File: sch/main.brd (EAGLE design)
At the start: 99.1 x 50.8 mm, 22 parts, among them IC2 PIC16F628P, K1 TF2--5V, K2 TF2--5V, T1 BC547, T2 BC547

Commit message: Better routing
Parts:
- moved R2 26.2 mm to (77.5, 19.1), turned to 0 degrees
- moved R3 9.16 mm to (59.7, 26.7), turned to 0 degrees
- moved C3 1.80 mm to (33.0, 31.8), turned to 90 degrees
- moved T1 1.27 mm to (82.5, 22.9)
- moved T2 1.27 mm to (64.8, 22.9)
- turned C1 to 90 degrees
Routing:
- net N$9: track 99.2 -> 3.81 mm
- net SW1: track 117.0 -> 26.8 mm, vias 2 -> 0
- net GND: track 342.9 -> 263.0 mm, vias 2 -> 0
- net N$8: track 75.8 -> 3.81 mm
- net DB0: track 77.3 -> 23.7 mm
- net DB1: track 67.2 -> 16.5 mm, vias 2 -> 0
- net +5V: track 167.8 -> 129.3 mm
- net +12V: track 113.7 -> 77.4 mm, vias 4 -> 1
- net N$2: track 49.7 -> 32.2 mm, vias 2 -> 0
- net N$6: track 3.81 -> 19.4 mm
- net SW3: track 61.3 -> 48.2 mm
- net N$1: track 32.1 -> 20.6 mm
- net RS: track 44.8 -> 38.1 mm, vias 2 -> 0
- net SW2: track 38.2 -> 34.3 mm, vias 2 -> 0
- net N$7: track 3.81 -> 6.33 mm
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
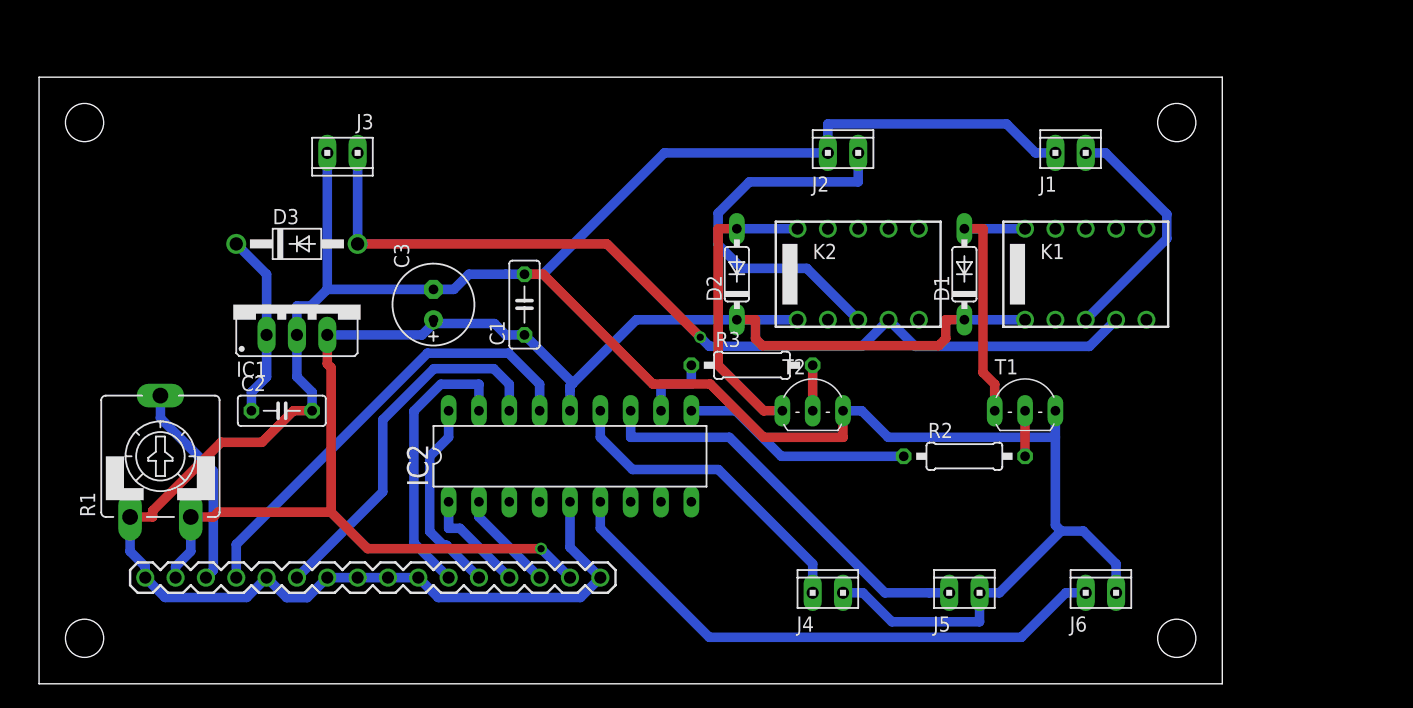
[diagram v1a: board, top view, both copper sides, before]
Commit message: Replaced relays with transistors
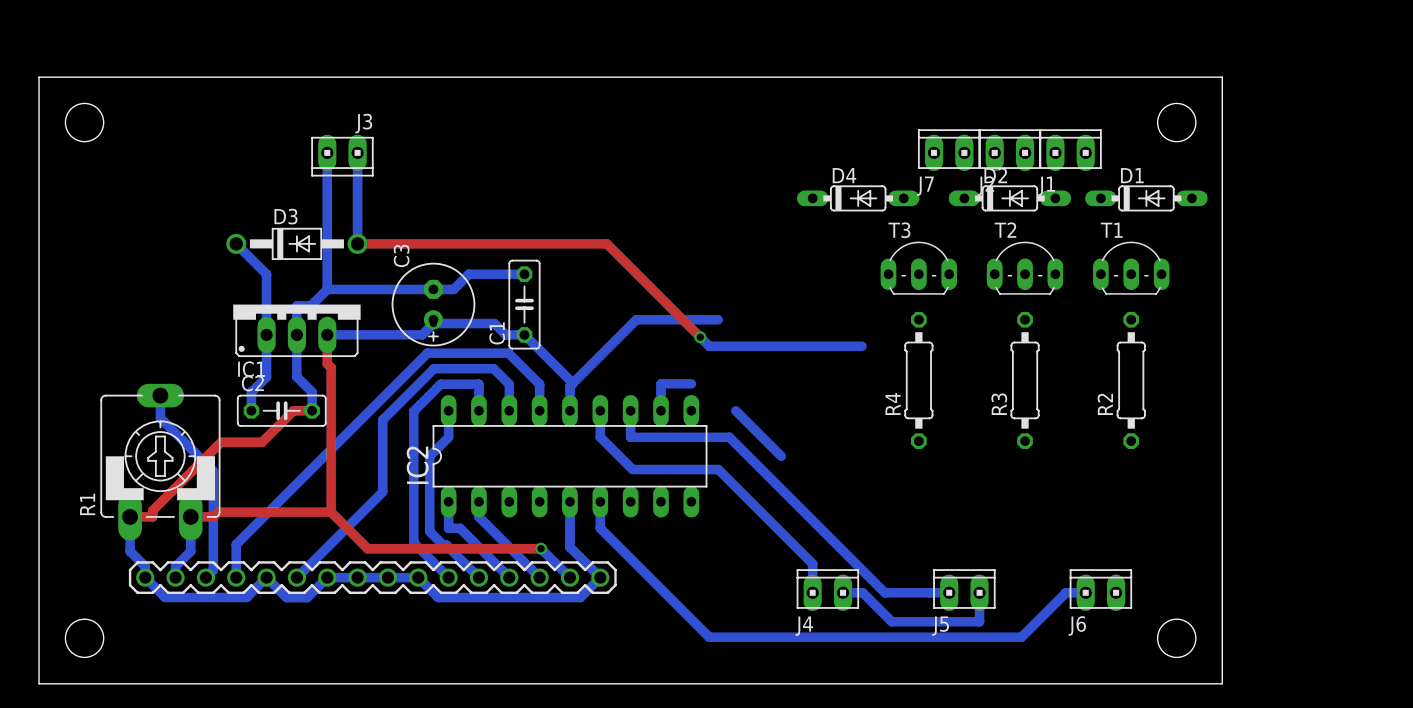
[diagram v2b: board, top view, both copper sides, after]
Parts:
- removed K1, K2: TF2--5V, relay:TF2
- added D4: 1N4148, diode:DO35-7
- added J7: (no value), con-amp:10X02MTA
- added R4: 4k7, rcl:0207/10
- added T3: BC337, transistor:TO92-CBE
- R2, R3: value 10k -> 4k7
- T1, T2: value BC547 -> BC337
- moved D2 23.7 mm to (81.3, 40.6), turned to 0 degrees
- moved R3 22.9 mm to (82.5, 25.4), turned to 90 degrees
- moved T2 21.1 mm to (82.5, 34.3)
- moved D1 16.5 mm to (92.7, 40.6), turned to 0 degrees
- moved R2 15.3 mm to (91.4, 25.4), turned to 90 degrees
- moved T1 14.5 mm to (91.4, 34.3)
- moved J2 14.0 mm to (81.3, 44.5)
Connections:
- removed net N$1 (its old number): J1.1, K1.3
- removed net N$4 (its old number): D1.A, K1.10, T1.C
- new net N$10: IC2.10, R3.1
- new net N$8: R4.2, T3.B
- new net N$9: D4.A, J7.2, T3.C
- net +12V: now also D1.C, D2.C, D4.C, J1.1, J2.1, J7.1; no longer K1.4, K2.4
- net +5V: no longer D1.C, D2.C, K1.1, K2.1
- net GND: now also T3.E; no longer J1.2, J2.2
- net N$2: now also D1.A, J1.2, T1.C; no longer J2.1, K2.3
- net N$5: now also J2.2; no longer K2.10
- net N$6: now also IC2.9; no longer IC2.10
- net N$7: now also R4.1; no longer R3.1
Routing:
- net GND: track 263.0 -> 130.2 mm
- net +5V: track 129.3 -> 94.9 mm
- net N$2: track 32.2 -> 0.00 mm
- net N$5: track 25.0 -> 0.00 mm
- net +12V: track 77.4 -> 53.4 mm
- net N$4 (its old number): track 22.3 -> 0.00 mm
- net N$1 (its old number): track 20.6 -> 0.00 mm
- net N$6: track 19.4 -> 5.39 mm
- net N$4: track 3.81 -> 0.00 mm
- net N$1: track 3.81 -> 0.00 mm
- net N$7: track 6.33 -> 4.77 mm

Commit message: First version for manufacturing
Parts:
- removed J1, J2, J3, J4, J5, J6, J7: (no value), con-amp:10X02MTA
- added S1, S2, S3: (no value), switch-omron:B3F-10XX
- added S4: (no value), switch:320-916
- added U1: LCD_BL_16X2_LOW, lcdmodules2:LCD_BL_16X2_LOW
- added X1: D-SUB9-H2M09ST, con-thomas-betts:H2M09ST
- U$1: value LCD_BL_16X2 -> KLDVX-0202-A; device lcdmodules:HEADER_16 -> con-kycon:KLDVX-0202-A
- moved R1 68.3 mm to (77.5, 7.62), flipped to the bottom, turned to 180 degrees
- moved D2 42.1 mm to (39.4, 44.5), turned to 270 degrees
- moved U$1 39.4 mm to (22.9, 45.7), flipped to the bottom
- moved T2 26.7 mm to (55.9, 35.6)
- moved R3 23.0 mm to (59.7, 27.9), turned to 180 degrees
- moved T1 17.8 mm to (73.7, 35.6)
- moved R2 17.8 mm to (73.7, 25.4)
- moved D1 16.9 mm to (76.2, 44.5), turned to 270 degrees
- moved D4 10.9 mm to (78.7, 44.5), turned to 270 degrees
- moved IC1 10.2 mm to (30.5, 26.7), flipped to the bottom, turned to 180 degrees
- moved R4 10.2 mm to (64.8, 30.5), turned to 0 degrees
- moved C1 8.89 mm to (49.5, 31.8)
- moved C2 8.89 mm to (29.2, 22.9)
- moved D3 8.89 mm to (30.5, 36.8)
- moved IC2 8.89 mm to (53.3, 19.1)
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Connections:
- new net N$12: S4.2, U$1.1
- net +12V: now also S4.3, X1.1, X1.3, X1.5; no longer J1.1, J2.1, J3.2, J7.1
- net +5V: now also U1.15, U1.2; no longer U$1.15, U$1.2
- net DB0: now also U1.11; no longer U$1.11
- net DB1: now also U1.12; no longer U$1.12
- net DB2: now also U1.13; no longer U$1.13
- net DB3: now also U1.14; no longer U$1.14
- net E: now also U1.6; no longer U$1.6
- net GND: now also S1.3, S1.4, S2.3, S2.4, S3.3, S3.4, U$1.2, U1.1, U1.10, U1.16, U1.5, U1.7, U1.8, U1.9; no longer J3.1, J4.1, J5.1, J6.1, U$1.1, U$1.10, U$1.16, U$1.5, U$1.7, U$1.8, U$1.9
- net N$11: now also U1.3; no longer U$1.3
- net N$2: now also X1.2; no longer J1.2
- net N$5: now also X1.4; no longer J2.2
- net N$9: now also X1.6; no longer J7.2
- net RS: now also U1.4; no longer U$1.4
- net SW1: now also S1.1, S1.2; no longer J4.2
- net SW2: now also S2.1, S2.2; no longer J5.2
- net SW3: now also S3.1, S3.2; no longer J6.2
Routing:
- net GND: track 130.2 -> 236.8 mm, vias 0 -> 2
- net E: track 31.3 -> 123.3 mm
- net +12V: track 53.4 -> 104.9 mm, vias 1 -> 0
- net N$12: track 0.00 -> 47.4 mm
- net DB0: track 23.7 -> 56.7 mm
- net SW1: track 26.8 -> 57.4 mm
- net N$5: track 0.00 -> 29.6 mm
- net DB1: track 16.5 -> 44.1 mm
- net N$9: track 0.00 -> 25.8 mm
- net DB3: track 8.45 -> 33.9 mm
- net N$2: track 0.00 -> 25.1 mm
- net N$11: track 17.3 -> 35.7 mm
- net DB2: track 9.01 -> 25.7 mm
- net RS: track 38.1 -> 24.6 mm, vias 0 -> 2
- net SW2: track 34.3 -> 45.9 mm, vias 0 -> 1
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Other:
- board size 99.1 x 50.8 mm -> 114.3 x 50.8 mm
- board text added: "BOT"
- board text added: "TOP"

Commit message: Updated 3d model
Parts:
- U1: value LCD_BL_16X2_LOW -> YM1602G_LOWCON; device lcdmodules2:LCD_BL_16X2_LOW -> lcdmodules2:YM1602G_LOWCON
- moved U1 34.9 mm to (48.9, 24.7)
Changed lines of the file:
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@@
 <?xml version="1.0" encoding="utf-8"?>
 <!DOCTYPE eagle SYSTEM "eagle.dtd">
-<eagle version="6.2">
+<eagle version="6.1">
 <drawing>
 <settings>
@@
 </element>
 <element name="S4" library="switch" package="320-916" value="" x="3.81" y="13.97"/>
-<element name="U1" library="lcdmodules2" package="LCD_BL_16X2_LOW" value="LCD_BL_16X2_LOW" x="17.78" y="8.89"/>
+<element name="U1" library="lcdmodules2" package="YM1602G_LOWCON" value="YM1602G_LOWCON" x="48.919590625" y="24.743953125"/>
 </elements>
 <signals>
@@
 <wire x1="98.6171" y1="23.1394" x2="98.6171" y2="38.3794" width="0.8" layer="16"/>
 <wire x1="101.0412" y1="38.3794" x2="98.6171" y2="38.3794" width="0.8" layer="16"/>
-<wire x1="98.6171" y1="23.1394" x2="96.9629" y2="23.1394" width="0.8" layer="16"/>
-<wire x1="94.5388" y1="23.1394" x2="96.9629" y2="23.1394" width="0.8" layer="16"/>
+<wire x1="94.5388" y1="23.1394" x2="98.6171" y2="23.1394" width="0.8" layer="16"/>
 <wire x1="98.6171" y1="7.8994" x2="94.5388" y2="7.8994" width="0.8" layer="16"/>
 <wire x1="101.0412" y1="7.8994" x2="98.6171" y2="7.8994" width="0.8" layer="16"/>
@@
 <wire x1="62.2014" y1="37.7809" x2="59.9805" y2="35.56" width="0.8" layer="1"/>
 <wire x1="94.5388" y1="7.8994" x2="92.1147" y2="7.8994" width="0.8" layer="1"/>
-<wire x1="50.8" y1="8.89" x2="50.8" y2="11.0981" width="0.8" layer="16"/>
+<wire x1="50.824590625" y1="8.868953125" x2="50.8" y2="11.0981" width="0.8" layer="16"/>
 <wire x1="50.8" y1="11.0981" x2="51.419" y2="11.0981" width="0.8" layer="16"/>
 <wire x1="51.419" y1="11.0981" x2="53.34" y2="13.0191" width="0.8" layer="16"/>
@@
 <wire x1="71.4374" y1="11.0981" x2="55.88" y2="11.0981" width="0.8" layer="16"/>
 <wire x1="53.34" y1="15.24" x2="53.34" y2="13.0191" width="0.8" layer="16"/>
-<wire x1="55.88" y1="8.89" x2="55.88" y2="11.0981" width="0.8" layer="16"/>
+<wire x1="55.904590625" y1="8.868953125" x2="55.88" y2="11.0981" width="0.8" layer="16"/>
 <wire x1="55.88" y1="11.0981" x2="53.959" y2="13.0191" width="0.8" layer="16"/>
 <wire x1="53.959" y1="13.0191" x2="53.34" y2="13.0191" width="0.8" layer="16"/>
@@
 <wire x1="31.75" y1="24.4205" x2="30.48" y2="25.6905" width="0.8" layer="16"/>
 <wire x1="30.48" y1="25.6905" x2="30.48" y2="29.21" width="0.8" layer="16"/>
-<wire x1="31.879" y1="22.86" x2="31.75" y2="22.86" width="0.8" layer="16"/>
-<wire x1="31.879" y1="22.86" x2="33.3105" y2="22.86" width="0.8" layer="16"/>
+<wire x1="31.75" y1="22.86" x2="33.3105" y2="22.86" width="0.8" layer="16"/>
 <wire x1="68.58" y1="35.56" x2="68.58" y2="33.3391" width="0.8" layer="16"/>
 <wire x1="76.2" y1="35.56" x2="76.2" y2="33.3391" width="0.8" layer="16"/>
@@
 <wire x1="47.9695" y1="34.29" x2="43.3197" y2="29.6402" width="0.8" layer="16"/>
 <wire x1="43.3197" y1="29.6402" x2="41.91" y2="29.6402" width="0.8" layer="16"/>
-<wire x1="40.64" y1="8.89" x2="40.64" y2="11.0981" width="0.8" layer="16"/>
-<wire x1="35.56" y1="8.89" x2="35.56" y2="11.0981" width="0.8" layer="16"/>
+<wire x1="40.664590625" y1="8.868953125" x2="40.64" y2="11.0981" width="0.8" layer="16"/>
+<wire x1="35.584590625" y1="8.868953125" x2="35.56" y2="11.0981" width="0.8" layer="16"/>
 <wire x1="35.56" y1="11.0981" x2="36.4981" y2="11.0981" width="0.8" layer="16"/>
 <wire x1="36.4981" y1="11.0981" x2="36.83" y2="11.43" width="0.8" layer="16"/>
-<wire x1="33.02" y1="8.89" x2="35.56" y2="8.89" width="0.8" layer="16"/>
+<wire x1="33.044590625" y1="8.868953125" x2="35.584590625" y2="8.868953125" width="0.8" layer="16"/>
 <via x="30.4665" y="36.9216" extent="1-16" drill="0.6096" diameter="1.016"/>
 <via x="36.83" y="11.43" extent="1-16" drill="0.8" diameter="1.2064"/>
@@
 <wire x1="36.83" y1="11.43" x2="40.3081" y2="11.43" width="0.8" layer="16"/>
 <wire x1="40.3081" y1="11.43" x2="40.64" y2="11.0981" width="0.8" layer="16"/>
-<wire x1="30.48" y1="8.89" x2="33.02" y2="8.89" width="0.8" layer="16"/>
-<wire x1="30.48" y1="8.89" x2="27.94" y2="8.89" width="0.8" layer="16"/>
+<wire x1="30.504590625" y1="8.868953125" x2="33.044590625" y2="8.868953125" width="0.8" layer="16"/>
+<wire x1="30.504590625" y1="8.868953125" x2="27.964590625" y2="8.868953125" width="0.8" layer="16"/>
 <wire x1="58.42" y1="35.56" x2="58.42" y2="35.1435" width="0.8" layer="16"/>
 <wire x1="58.42" y1="35.1435" x2="56.6156" y2="33.3391" width="0.8" layer="16"/>
@@
 <wire x1="78.1193" y1="12.1831" x2="78.1193" y2="12.7" width="0.8" layer="16"/>
 <wire x1="53.34" y1="7.007" x2="53.34" y2="6.6819" width="0.8" layer="16"/>
-<wire x1="53.34" y1="8.89" x2="53.34" y2="7.007" width="0.8" layer="16"/>
-<wire x1="48.26" y1="8.89" x2="48.26" y2="6.6819" width="0.8" layer="16"/>
+<wire x1="53.364590625" y1="8.868953125" x2="53.34" y2="7.007" width="0.8" layer="16"/>
+<wire x1="48.284590625" y1="8.868953125" x2="48.26" y2="6.6819" width="0.8" layer="16"/>
 <wire x1="53.34" y1="6.6819" x2="48.26" y2="6.6819" width="0.8" layer="16"/>
 <wire x1="39.37" y1="27.94" x2="35.9521" y2="27.94" width="0.8" layer="1"/>
@@
 <contactref element="U1" pad="11"/>
 <wire x1="45.72" y1="22.86" x2="45.72" y2="25.0809" width="0.8" layer="16"/>
-<wire x1="25.4" y1="8.89" x2="25.4" y2="6.6819" width="0.8" layer="16"/>
+<wire x1="25.424590625" y1="8.868953125" x2="25.4" y2="6.6819" width="0.8" layer="16"/>
 <wire x1="25.4" y1="6.6819" x2="24.0999" y2="5.3818" width="0.8" layer="16"/>
 <wire x1="24.0999" y1="5.3818" x2="16.5481" y2="5.3818" width="0.8" layer="16"/>
@@
 <contactref element="IC2" pad="18"/>
 <contactref element="U1" pad="12"/>
-<wire x1="22.86" y1="8.89" x2="22.86" y2="6.6819" width="0.8" layer="16"/>
+<wire x1="22.884590625" y1="8.868953125" x2="22.86" y2="6.6819" width="0.8" layer="16"/>
 <wire x1="22.86" y1="6.6819" x2="17.0866" y2="6.6819" width="0.8" layer="16"/>
 <wire x1="17.0866" y1="6.6819" x2="16.1944" y2="7.5741" width="0.8" layer="16"/>
@@
 <contactref element="IC2" pad="1"/>
 <contactref element="U1" pad="13"/>
-<wire x1="20.32" y1="8.89" x2="20.32" y2="9.2362" width="0.8" layer="16"/>
+<wire x1="20.344590625" y1="8.868953125" x2="20.32" y2="9.2362" width="0.8" layer="16"/>
 <wire x1="20.32" y1="9.2362" x2="24.854" y2="13.7702" width="0.8" layer="16"/>
 <wire x1="24.854" y1="13.7702" x2="41.7102" y2="13.7702" width="0.8" layer="16"/>
@@
 <contactref element="U1" pad="14"/>
 <wire x1="45.72" y1="15.24" x2="45.72" y2="17.4609" width="0.8" layer="16"/>
-<wire x1="17.78" y1="8.89" x2="17.78" y2="9.2617" width="0.8" layer="16"/>
+<wire x1="17.804590625" y1="8.868953125" x2="17.78" y2="9.2617" width="0.8" layer="16"/>
 <wire x1="17.78" y1="9.2617" x2="23.6261" y2="15.1078" width="0.8" layer="16"/>
 <wire x1="23.6261" y1="15.1078" x2="40.17" y2="15.1078" width="0.8" layer="16"/>
@@
 <contactref element="U1" pad="6"/>
 <wire x1="48.26" y1="22.86" x2="48.26" y2="25.0809" width="0.8" layer="16"/>
-<wire x1="38.1" y1="8.89" x2="38.1" y2="6.6819" width="0.8" layer="16"/>
+<wire x1="38.124590625" y1="8.868953125" x2="38.1" y2="6.6819" width="0.8" layer="16"/>
 <wire x1="38.1" y1="6.6819" x2="35.4998" y2="4.0817" width="0.8" layer="16"/>
 <wire x1="35.4998" y1="4.0817" x2="13.805" y2="4.0817" width="0.8" layer="16"/>
@@
 <wire x1="42.1372" y1="12.3586" x2="39.3961" y2="15.0997" width="0.8" layer="1"/>
 <wire x1="39.3961" y1="15.0997" x2="39.3961" y2="16.6997" width="0.8" layer="1"/>
-<wire x1="43.18" y1="8.89" x2="43.18" y2="11.3158" width="0.8" layer="16"/>
+<wire x1="43.204590625" y1="8.868953125" x2="43.18" y2="11.3158" width="0.8" layer="16"/>
 <wire x1="43.18" y1="11.3158" x2="42.1372" y2="12.3586" width="0.8" layer="16"/>
 <wire x1="50.8" y1="20.6391" x2="43.3355" y2="20.6391" width="0.8" layer="16"/>
@@
 <contactref element="R1" pad="S"/>
 <contactref element="U1" pad="3"/>
-<wire x1="45.72" y1="8.89" x2="45.72" y2="6.6819" width="0.8" layer="16"/>
+<wire x1="45.744590625" y1="8.868953125" x2="45.72" y2="6.6819" width="0.8" layer="16"/>
 <wire x1="45.72" y1="6.6819" x2="49.8619" y2="2.54" width="0.8" layer="16"/>
 <wire x1="49.8619" y1="2.54" x2="77.47" y2="2.54" width="0.8" layer="16"/>

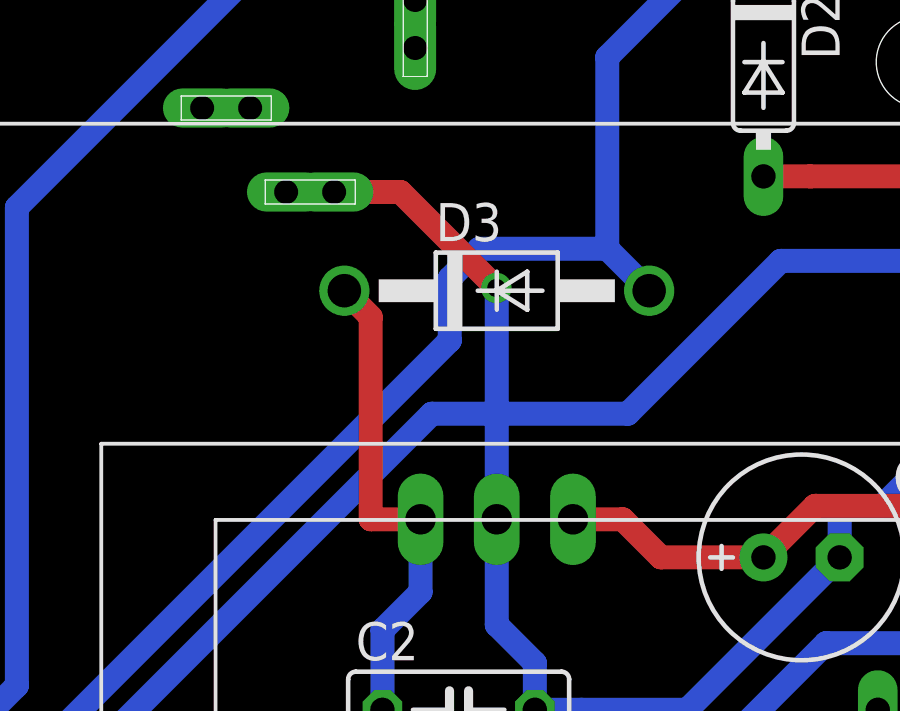
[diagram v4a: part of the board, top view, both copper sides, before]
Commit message: Removed short of GND and E
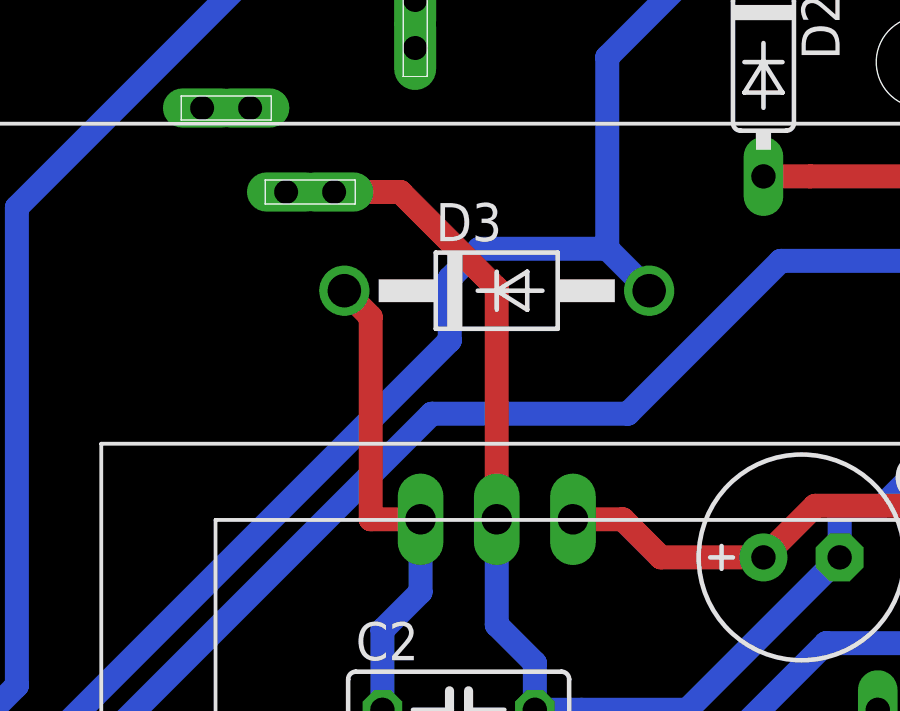
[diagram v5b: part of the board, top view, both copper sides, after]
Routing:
- net GND: vias 2 -> 1
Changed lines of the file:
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@@
 <?xml version="1.0" encoding="utf-8"?>
 <!DOCTYPE eagle SYSTEM "eagle.dtd">
-<eagle version="6.1">
+<eagle version="6.2">
 <drawing>
 <settings>
@@
 <wire x1="53.959" y1="13.0191" x2="53.34" y2="13.0191" width="0.8" layer="16"/>
 <wire x1="25.06" y1="40.12" x2="27.2681" y2="40.12" width="0.8" layer="1"/>
-<wire x1="27.2681" y1="40.12" x2="30.4665" y2="36.9216" width="0.8" layer="1"/>
-<wire x1="30.48" y1="29.21" x2="30.48" y2="36.9081" width="0.8" layer="16"/>
-<wire x1="30.48" y1="36.9081" x2="30.4665" y2="36.9216" width="0.8" layer="16"/>
+<wire x1="27.2681" y1="40.12" x2="30.48" y2="36.9081" width="0.8" layer="1"/>
+<wire x1="30.48" y1="29.21" x2="30.48" y2="36.9081" width="0.8" layer="1"/>
 <wire x1="31.75" y1="22.86" x2="31.75" y2="24.4205" width="0.8" layer="16"/>
 <wire x1="31.75" y1="24.4205" x2="30.48" y2="25.6905" width="0.8" layer="16"/>
@@
 <wire x1="36.4981" y1="11.0981" x2="36.83" y2="11.43" width="0.8" layer="16"/>
 <wire x1="33.044590625" y1="8.868953125" x2="35.584590625" y2="8.868953125" width="0.8" layer="16"/>
-<via x="30.4665" y="36.9216" extent="1-16" drill="0.6096" diameter="1.016"/>
 <via x="36.83" y="11.43" extent="1-16" drill="0.8" diameter="1.2064"/>
 <wire x1="31.75" y1="22.86" x2="31.75" y2="16.51" width="0.8" layer="1"/>
